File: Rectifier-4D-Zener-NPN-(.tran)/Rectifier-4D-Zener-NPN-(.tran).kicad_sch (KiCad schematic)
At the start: 13 parts, among them Q1 BDX53C

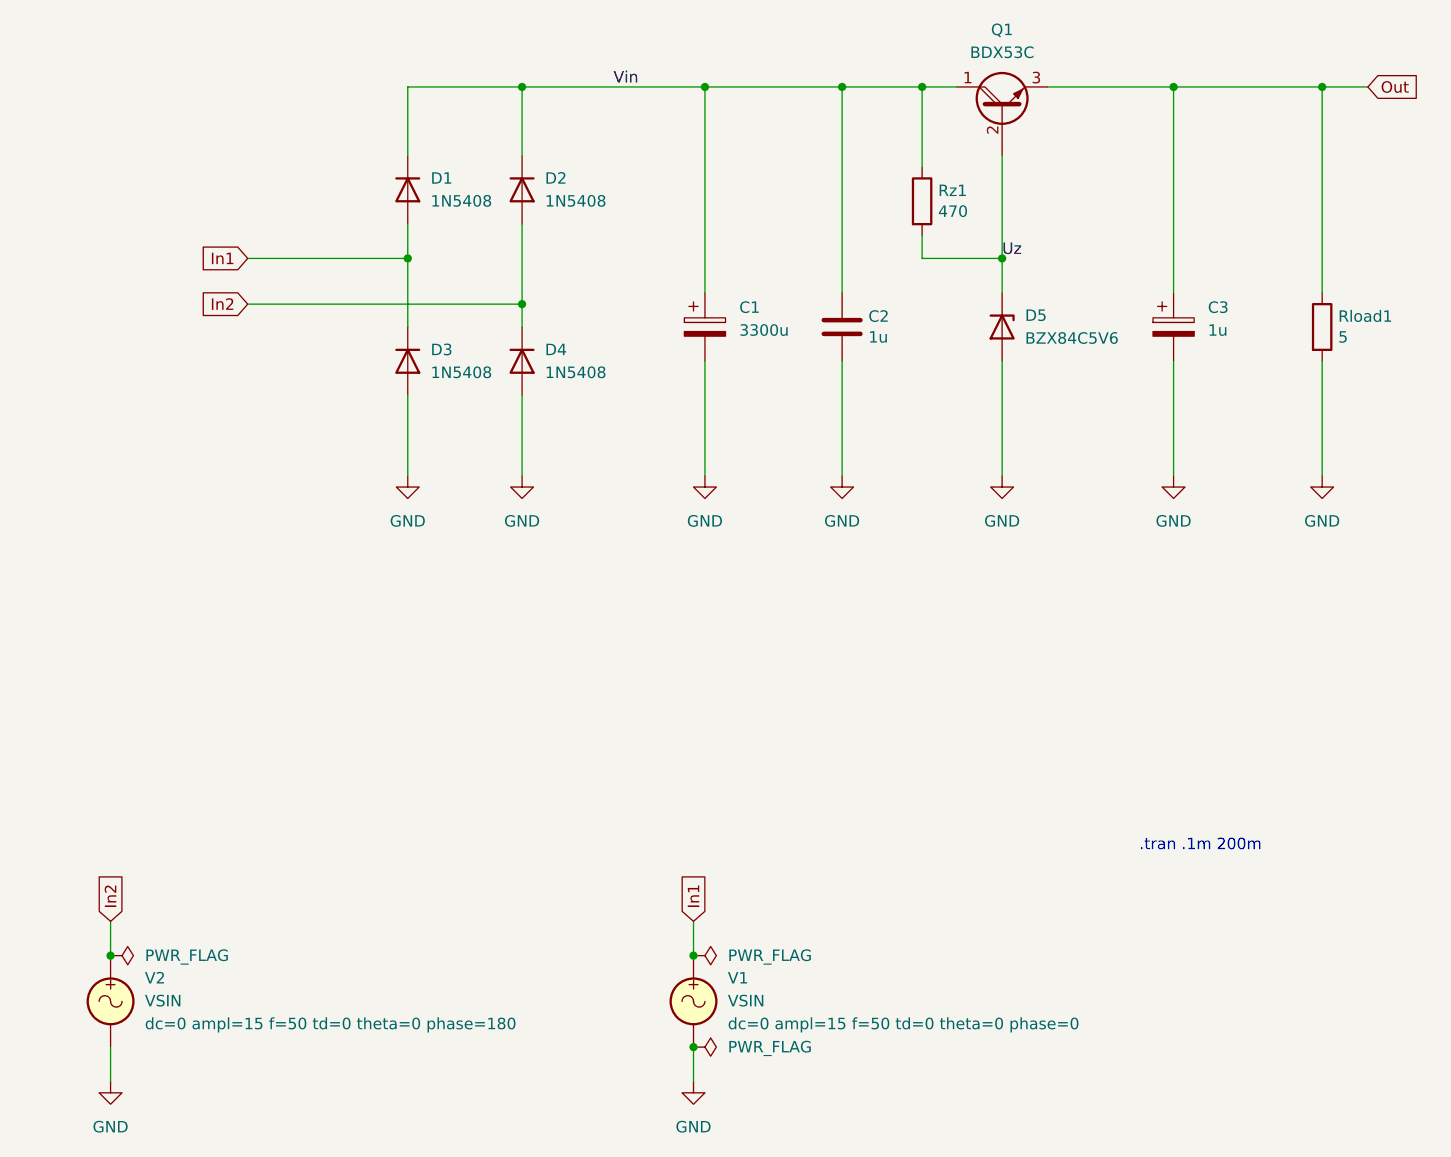
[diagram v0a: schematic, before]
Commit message: Updated all schematics and prepared for KiCad 8.0
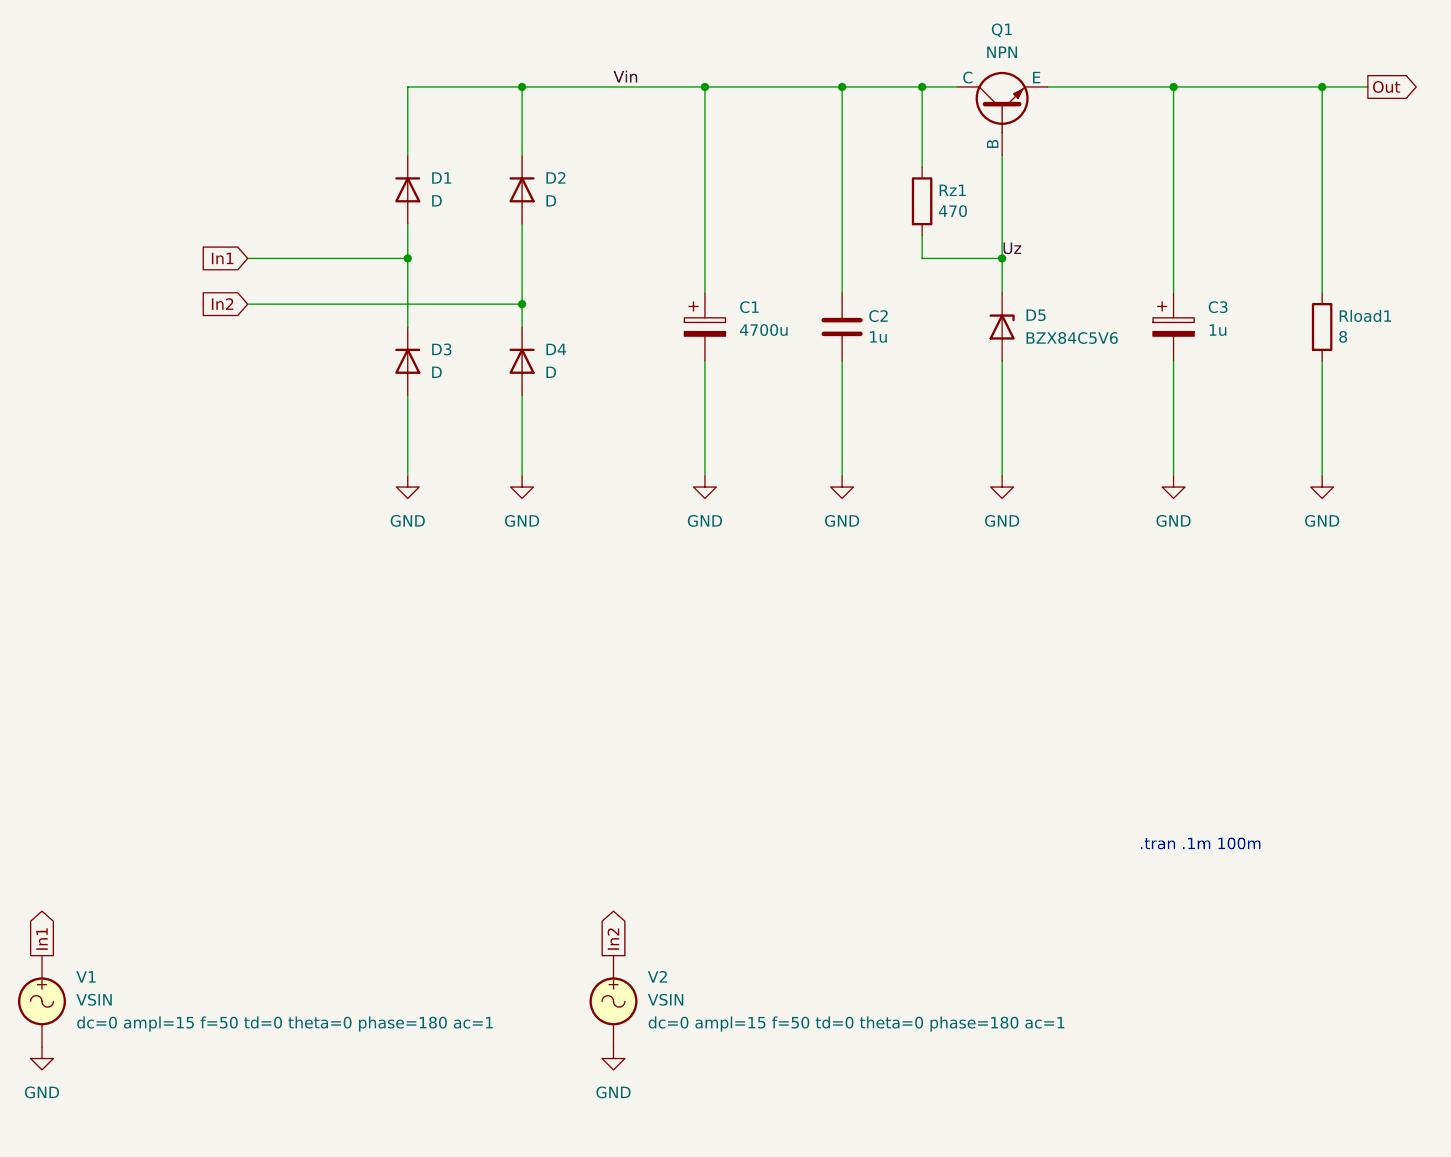
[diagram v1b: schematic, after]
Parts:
- removed Q1: BDX53C, symbol Device:Q_NPN_Darlington_CBE
- added Q1: NPN, symbol Simulation_SPICE:NPN
- C1: value 3300u -> 4700u
- D1, D2, D3, D4: value 1N5408 -> D
- Rload1: value 5 -> 8
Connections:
- net Out: now also Q1.3 (E)
- net Uz: now also Q1.2 (B)
- net Vin: now also Q1.1 (C)
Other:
- note added: ".tran .1m 100m"
- note removed: ".tran .1m 200m"
